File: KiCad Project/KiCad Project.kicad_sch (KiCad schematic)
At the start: 14 parts, among them U1 STM32F103C8T6, Y1 ECS-2520MV-160-CN-TR

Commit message: 2025/11/21
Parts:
- removed C5: 10u, symbol Device:C
- added C10: 10u, symbol Device:C
- added C11: 22u, symbol Device:C
- added C5: 10u, symbol Device:C_Polarized_US
- added J1: USB_C_Receptacle_USB2.0_16P, symbol Connector:USB_C_Receptacle_USB2.0_16P
- added R2, R3: 5k1, symbol Device:R
- added U5: AZ1117CH2-3.3, Package_TO_SOT_SMD:SOT-223-3_TabPin2, symbol Regulator_Linear:AZ1117CH2-3.3
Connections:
- net STM_OSC_IN is gone; now on net STM_OSC IN: Y1.1 (Tri-State)
- net STM_OSC_OUT is gone; now on net STM_OSC OUT: Y1.3 (OUT)
- net +3.3V: now also C11.1, C5.1, U5.3 (OUT)
- net GND: now also C9.1, R1.1, C10.2, C11.2, C5.2, J1.A1 (GND), J1.A12 (GND), J1.B1 (GND), J1.B12 (GND), R2.1, R3.1, U5.2 (GND)
- net STM_USB_D+: now also J1.A6 (D+), J1.B6 (D+)
- net STM_USB_D-: now also J1.A7 (D-), J1.B7 (D-)
- net STM_SCK: now reaches U1.15 (PA5)
- net STM_MISO: now reaches U1.16 (PA6)
- net STM_MOSI: now reaches U1.17 (PA7)
- net STM_SCL: now reaches U1.42 (PB6)
- net STM_SDA: now reaches U1.43 (PB7)
- new net: J1.B5 (CC2), R3.2
- new net: J1.A5 (CC1), R2.2
- new net VBUS: C10.1, J1.A4 (VBUS), J1.A9 (VBUS), J1.B4 (VBUS), J1.B9 (VBUS), U5.1 (IN)
- no-connect marks 0 -> 3
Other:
- note added: "C10 & C11 ESR < 20R"

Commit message: 2025/11/22
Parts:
- added C13: 2.2u, symbol Device:C
- added C14, C16, C17, C18, C19, C20, C24: 100n, symbol Device:C
- added C15: 10n, symbol Device:C
- added C21, C22, C23: 22u, symbol Device:C
- added D1: SMF5V0A, Diode_SMD:D_SMF, symbol Diode:SMF5V0A
- added F1: 0ZRG0120FF1E, 0ZRG0120FF1E:FUSRB510W51L690T300H1170, symbol 0ZRG0120FF1E:0ZRG0120FF1E
- added J2: XT30PW-M, XT30PW-M:AMASS_XT30PW-M, symbol XT30PW-M:XT30PW-M
- added L1: 2R2, symbol Device:L
- added Q1: CSD23280F3, CSD23280F3:TRANS_CSD23280F3, symbol CSD23280F3:CSD23280F3
- added U2: ICM-42670-P, ICM-42670-P:XDCR_ICM-42670-P, symbol ICM-42670-P:ICM-42670-P
- added U3: BME280, Package_LGA:Bosch_LGA-8_2.5x2.5mm_P0.65mm_ClockwisePinNumbering, symbol Sensor:BME280
- added U4: AP63203WU, Package_TO_SOT_SMD:TSOT-23-6, symbol Regulator_Switching:AP63203WU
- added U6: ESD122DMXR, ESD122DMXR:IC_ESD122DMXR, symbol ESD122DMXR:ESD122DMXR
- added U7: TPD1E10B09DPYR, TPD1E10B09DPYR:DIO_TPD1E10B09DPYR, symbol TPD1E10B09DPYR:TPD1E10B09DPYR
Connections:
- net GND is gone; now on net +3.3V: C1.2, C10.2, C11.2, C12.2, C2.2, C3.2, C4.2, C5.2, C6.2, C7.2, C8.2, C9.1, C9.2, J1.A1 (GND), J1.A12 (GND), J1.B1 (GND), J1.B12 (GND), R1.1, R2.1, R3.1, U1.23 (VSS), U1.35 (VSS), U1.47 (VSS), U1.8 (VSSA), U5.2 (GND), Y1.2 (GND)
- net +3.3V: now also C13.1, C13.2, C14.1, C14.2, C15.1, C15.2, C16.1, C16.2, C17.2, C18.1, C18.2, C19.2, C21.1, C21.2, C22.1, C22.2, C23.2, C24.2, D1.1 (A1), J2.N, L1.2, Q1.1, U2.1 (AP_SDO/AP_AD0), U2.12 (AP_CS), U2.5 (VDDIO), U2.6 (GND), U2.8 (VDD), U3.1 (GND), U3.5 (SDO), U3.7 (GND), U3.8 (VDD), U4.1 (FB), U4.4 (GND), U6.1 (GND), U7.2
- net STM_SCL: now also U2.13 (AP_SCL/AP_SCLK), U3.4 (SCK)
- net STM_SDA: now also U2.14 (AP_SDA/AP_SDIO/AP_SDI), U3.3 (SDI)
- net STM_USB_D+: now also U6.2 (IO1)
- net STM_USB_D-: now also U6.3 (IO2)
- net VBUS: now also D1.2 (A2)
- net STM_SWDIO: now reaches U1.34 (PA13)
- net STM_SWCLK: now reaches U1.37 (PA14)
- new net: C20.1, L1.1, U4.5 (SW)
- new net: C20.2, U4.6 (BST)
- new net: F1.1, Q1.2
- new net: C17.1, U3.2 (CSB), U3.6 (VDDIO)
- new net +7.5V: F1.2, J2.P, U7.1
- new net +BATT: C19.1, C23.1, C24.1, Q1.3, U4.2 (EN), U4.3 (IN)
- new net IMU_FSYNC: U2.7 (FSYNC)
- new net IMU_INT: U2.4 (INT1/INT)
- no-connect marks 3 -> 8
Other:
- note added: "16 MHz CMOS Oscillator"
- note added: "5V IN -> 3.3V OUT"
- note added: "Battery Connector - TVS, Fuse & Polarity"
- note added: "Buck Converter"
- note added: "IMU - Gyroscope & Accelerometer"
- note added: "L = (3.3V)(8.4V - 3.3V) / (8.4V)(1A)(1.1 * 10^6 MHz)"
- note added: "L = 1.823 uH -> 2.2 uH (Standard value)"
- note added: "L = Vout(Vin-Vout) / Vin*I*f"
- note added: "MCU"
- note added: "MCU Oscillator"
- note added: "Temperature, Pressure and Humidity Sensor"
- note added: "USB Type C Connector with TVS"
- note added: "Voltage Regulator"
- moved on the sheet: C1, C10, C11, C12, C2, C3, C4, C5, C6, C7, C8, C9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

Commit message: 2025/09/12
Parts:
- removed C1, C12, C14, C16, C17, C18, C19, C2, C20, C24, C3, C4, C9: 100n, symbol Device:C
- removed C10: 10u, symbol Device:C
- removed C11, C21, C22, C23: 22u, symbol Device:C
- removed C13: 2.2u, symbol Device:C
- removed C15, C6: 10n, symbol Device:C
- removed C5: 10u, symbol Device:C_Polarized_US
- removed C7, C8: 1u, symbol Device:C
- removed D1: SMF5V0A, Diode_SMD:D_SMF, symbol Diode:SMF5V0A
- removed F1: 0ZRG0120FF1E, 0ZRG0120FF1E:FUSRB510W51L690T300H1170, symbol 0ZRG0120FF1E:0ZRG0120FF1E
- removed FB1: 120R, symbol Device:FerriteBead
- removed J1: USB_C_Receptacle_USB2.0_16P, symbol Connector:USB_C_Receptacle_USB2.0_16P
- removed J2: XT30PW-M, XT30PW-M:AMASS_XT30PW-M, symbol XT30PW-M:XT30PW-M
- removed L1: 2R2, symbol Device:L
- removed Q1: CSD23280F3, CSD23280F3:TRANS_CSD23280F3, symbol CSD23280F3:CSD23280F3
- removed R1: 10k, symbol Device:R
- removed R2, R3: 5k1, symbol Device:R
- removed U1: STM32F103C8T6, Package_QFP:LQFP-48_7x7mm_P0.5mm, symbol MCU_ST_STM32F1:STM32F103C8Tx
- removed U2: ICM-42670-P, ICM-42670-P:XDCR_ICM-42670-P, symbol ICM-42670-P:ICM-42670-P
- removed U3: BME280, Package_LGA:Bosch_LGA-8_2.5x2.5mm_P0.65mm_ClockwisePinNumbering, symbol Sensor:BME280
- removed U4: AP63203WU, Package_TO_SOT_SMD:TSOT-23-6, symbol Regulator_Switching:AP63203WU
- removed U5: AZ1117CH2-3.3, Package_TO_SOT_SMD:SOT-223-3_TabPin2, symbol Regulator_Linear:AZ1117CH2-3.3
- removed U6: ESD122DMXR, ESD122DMXR:IC_ESD122DMXR, symbol ESD122DMXR:ESD122DMXR
- removed U7: TPD1E10B09DPYR, TPD1E10B09DPYR:DIO_TPD1E10B09DPYR, symbol TPD1E10B09DPYR:TPD1E10B09DPYR
- removed Y1: ECS-2520MV-160-CN-TR, Oscillator:Oscillator_SMD_ECS_2520MV-xxx-xx-4Pin_2.5x2.0mm, symbol Oscillator:ECS-2520MV-xxx-xx
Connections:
- no-connect marks 8 -> 0
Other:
- added sheet Datalogging (HPRFC_Sheet4_Datalogging.kicad_sch)
- added sheet MCU (HPRFC_Sheet1_MCU.kicad_sch)
- added sheet Power & Connectors (HPRFC_Sheet2_Power&Connectors.kicad_sch)
- added sheet Sensors (HPRFC_Sheet3_Sensors.kicad_sch)
- note added: "High Power Rocket Flight Computer"
- note removed: "16 MHz CMOS Oscillator"
- note removed: "5V IN -> 3.3V OUT"
- note removed: "Battery Connector - TVS, Fuse & Polarity"
- note removed: "Buck Converter"
- note removed: "C10 & C11 ESR < 20R"
- note removed: "IMU - Gyroscope & Accelerometer"
- note removed: "L = (3.3V)(8.4V - 3.3V) / (8.4V)(1A)(1.1 * 10^6 MHz)"
- note removed: "L = 1.823 uH -> 2.2 uH (Standard value)"
- note removed: "L = Vout(Vin-Vout) / Vin*I*f"
- note removed: "MCU"
- note removed: "MCU Oscillator"
- note removed: "Temperature, Pressure and Humidity Sensor"
- note removed: "USB Type C Connector with TVS"
- note removed: "Voltage Regulator"
- company: (none) -> Edward Sicoe
- title: (none) -> High Power Rocket Flight Computer - Hierarchical Page

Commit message: Datasheet renaming and schematic formatting, text, tables, etc.
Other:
- sheet Datalogging: file HPRFC_Sheet4_Datalogging.kicad_sch -> STMRocket_Sheet4_Datalogging.kicad_sch
- sheet MCU: file HPRFC_Sheet1_MCU.kicad_sch -> STMRocket_Sheet1_MCU.kicad_sch
- sheet Power & Connectors: file HPRFC_Sheet2_Power&Connectors.kicad_sch -> STMRocket_Sheet2_Power&Connectors.kicad_sch
- sheet Sensors: file HPRFC_Sheet3_Sensors.kicad_sch -> STMRocket_Sheet3_Sensors.kicad_sch
- note added: "About"
- note added: "Project Description This is a personal project for an STM32 flight computer that will be flown on a model rocket to acheive the Level 1 high power rocketry certification. It is open source with details available on the Github repository. https://github.com/esicoe/STMRocket Capabilities The flight computer is able to log flight condition data, including pressure, altitude, acceleration, gyroscope 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"
- note added: "Revision History"
- note added: "STMRocket (2025/12/09 by Edward S.)"
- note added: "The datalogging chips are: 4 Mb of NOR flash memory which is programmed and communicates over 3 wire SPI at 2MHz. The MicroSD card does not operate in flight. It is a way to extract the data from the onboard memory."
- note added: "The sensors are: IMU IC (Intertial measurement units) which contains a programmable gyroscope, accelerometer and data filter. Environmental sensor that contains a programmable pressure, humidity, and temperature measurements with a filter. All sensors are programmed and communicate over I2C at 100kHz."
- note removed: "High Power Rocket Flight Computer"
- title: High Power Rocket Flight Computer - Hierarchical Page -> STMRocket - Main Page

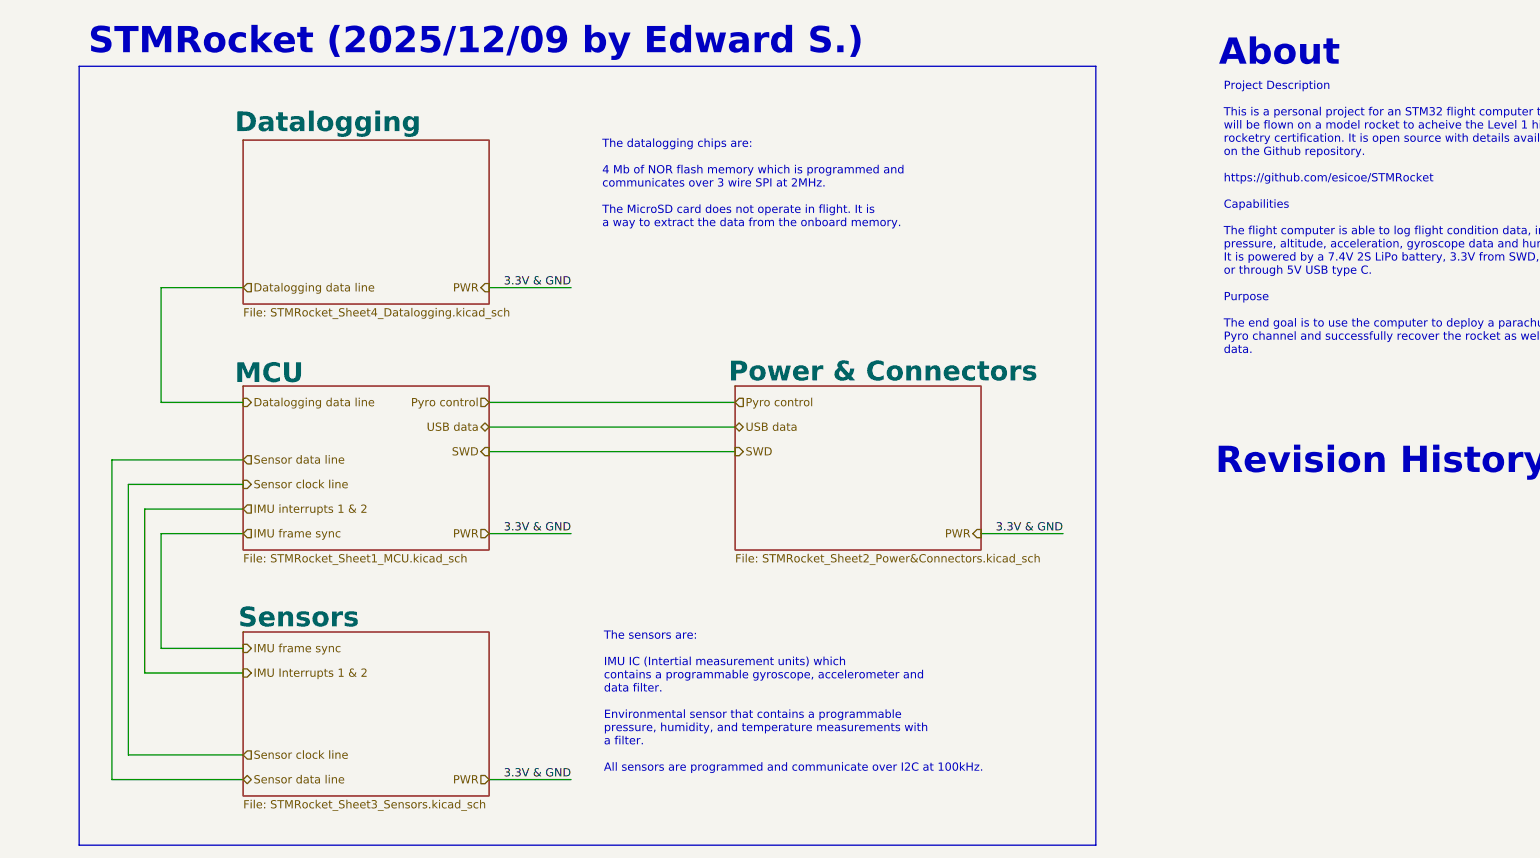
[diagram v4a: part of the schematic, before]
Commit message: Updated layout, documentation and schematic. Component placement finished.
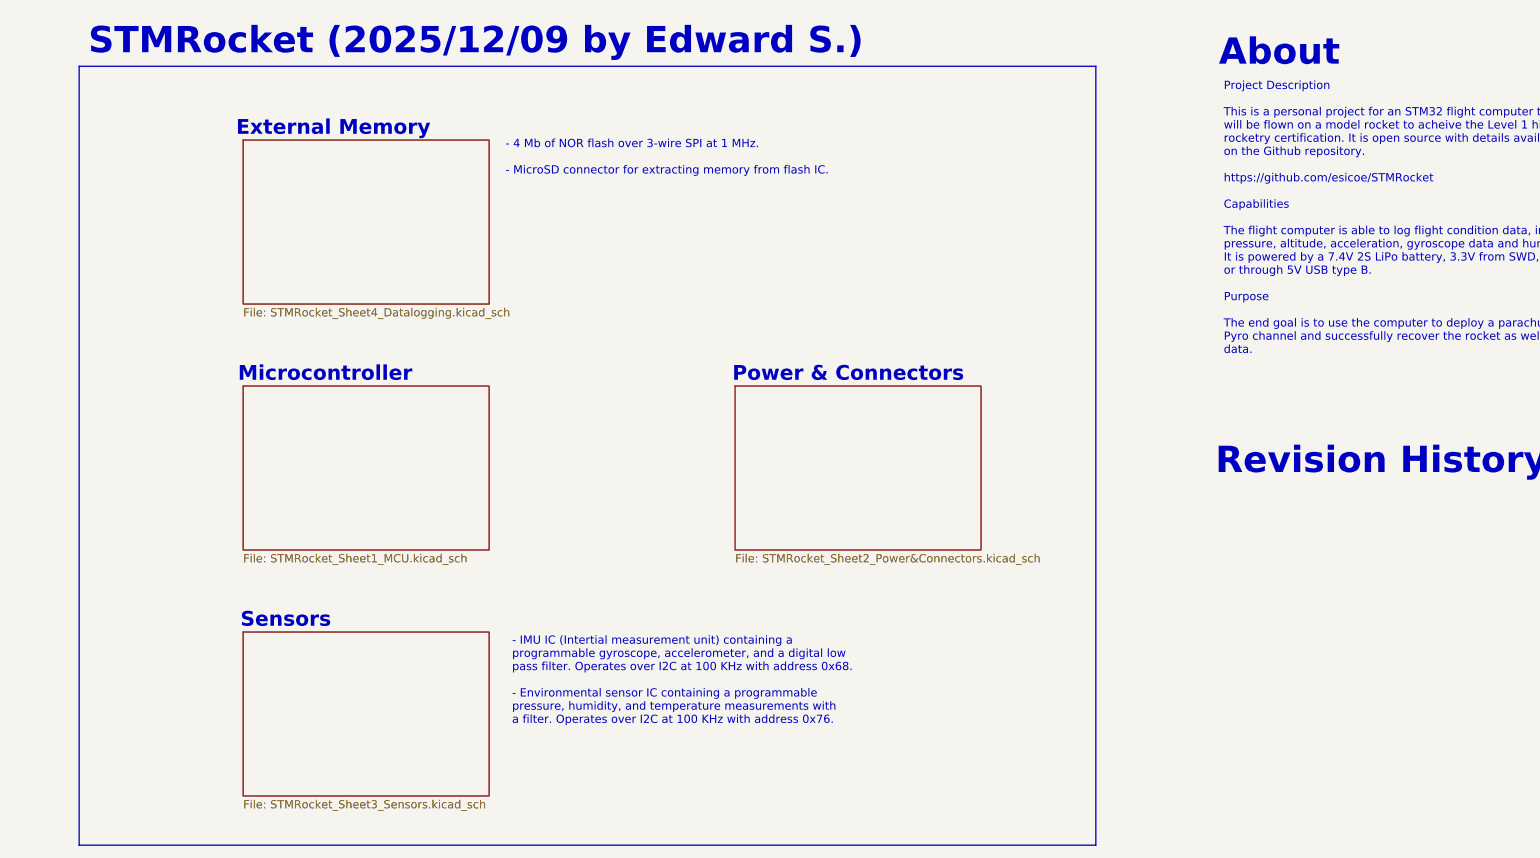
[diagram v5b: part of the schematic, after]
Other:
- note added: "- 4 Mb of NOR flash over 3-wire SPI at 1 MHz. - MicroSD connector for extracting memory from flash IC."
- note added: "- IMU IC (Intertial measurement unit) containing a programmable gyroscope, accelerometer, and a digital low pass filter. Operates over I2C at 100 KHz with address 0x68. - Environmental sensor IC containing a programmable pressure, humidity, and temperature measurements with a filter. Operates over I2C at 100 KHz with address 0x76."
- note added: "External Memory"
- note added: "Microcontroller"
- note added: "Power & Connectors"
- note added: "Sensors"
- note removed: "The datalogging chips are: 4 Mb of NOR flash memory which is programmed and communicates over 3 wire SPI at 2MHz. The MicroSD card does not operate in flight. It is a way to extract the data from the onboard memory."
- note removed: "The sensors are: IMU IC (Intertial measurement units) which contains a programmable gyroscope, accelerometer and data filter. Environmental sensor that contains a programmable pressure, humidity, and temperature measurements with a filter. All sensors are programmed and communicate over I2C at 100kHz."
